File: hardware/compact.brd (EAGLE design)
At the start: 54 x 59 mm, 26 parts, among them SW1 SWITCH_SPDT, U1 MCP73831, U2 EDISON_CONNECTOR_FULLMOUNTING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, U3 EDISON_CONNECTOR_FULLHEADER

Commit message: add USB data lines, use 1.8v line, not vcc, for Max3218, DRC fixes
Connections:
- net 1.8V: now also B78108S1153K.2, C4.1, MAX3218.4, MAX3218.6
- net USB_DN: now also JP1.D-1
- net USB_DP: now also JP1.D+1
- net USB_ID: now also JP1.ID1
- net VSYS: no longer B78108S1153K.2, C4.1, MAX3218.4, MAX3218.6
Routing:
- net 1.8V: track 4.22 -> 47.1 mm
- net USB_ID: track 3.33 -> 42.9 mm
- net USB_DP: track 6.60 -> 45.7 mm, vias 1 -> 2
- net USB_DN: track 9.44 -> 46.3 mm, vias 1 -> 2
- net VSYS: track 96.0 -> 69.9 mm
- net N$11: track 15.8 -> 30.4 mm
- net 1: track 6.96 -> 13.7 mm
- net N$10: track 19.3 -> 16.0 mm
- net VBAT: track 33.8 -> 36.1 mm, vias 1 -> 0
- net T1OUT: track 23.5 -> 24.4 mm
- net GP134_UART_2_RX: track 55.2 -> 56.0 mm
- net 3.3V: track 7.49 -> 8.27 mm
- net N$6: track 3.96 -> 3.33 mm
- net CX: track 35.5 -> 36.0 mm

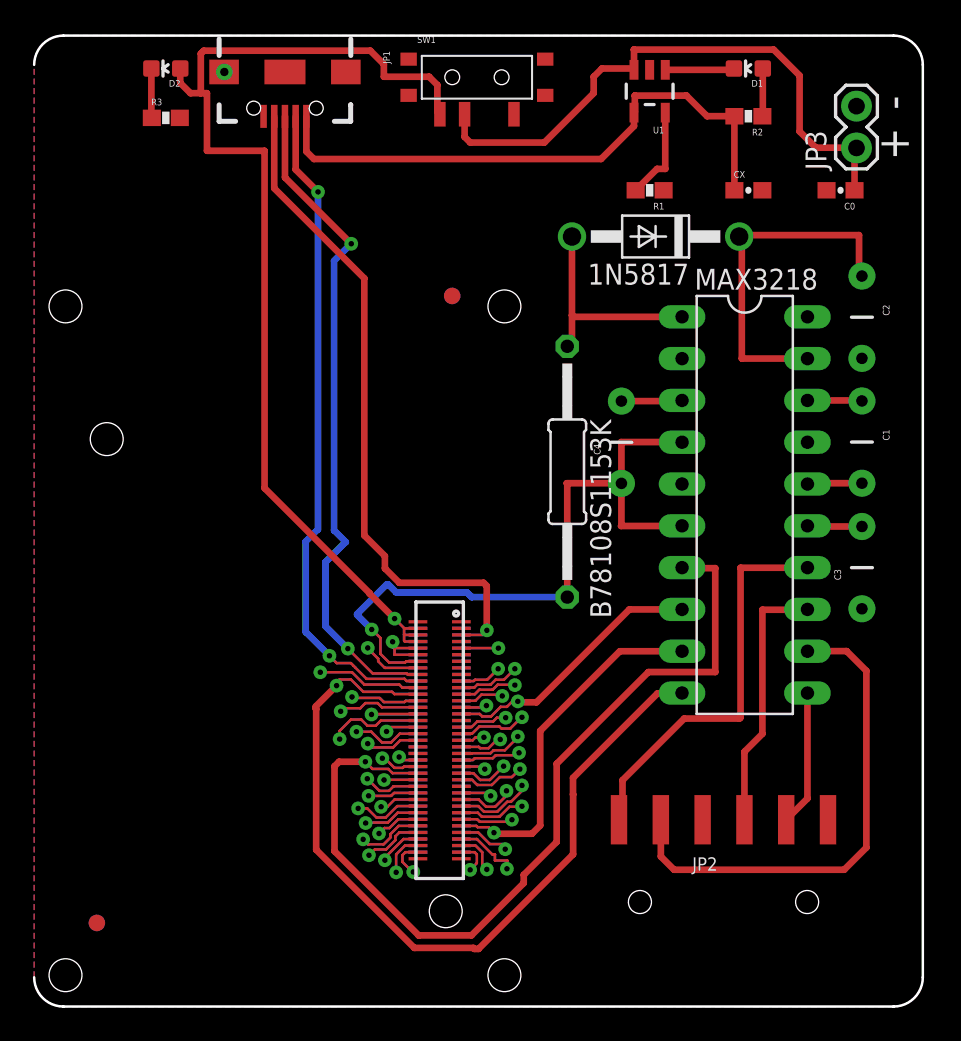
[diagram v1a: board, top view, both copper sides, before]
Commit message: Update readme, board routing fixes, change LED names to functions vice colors
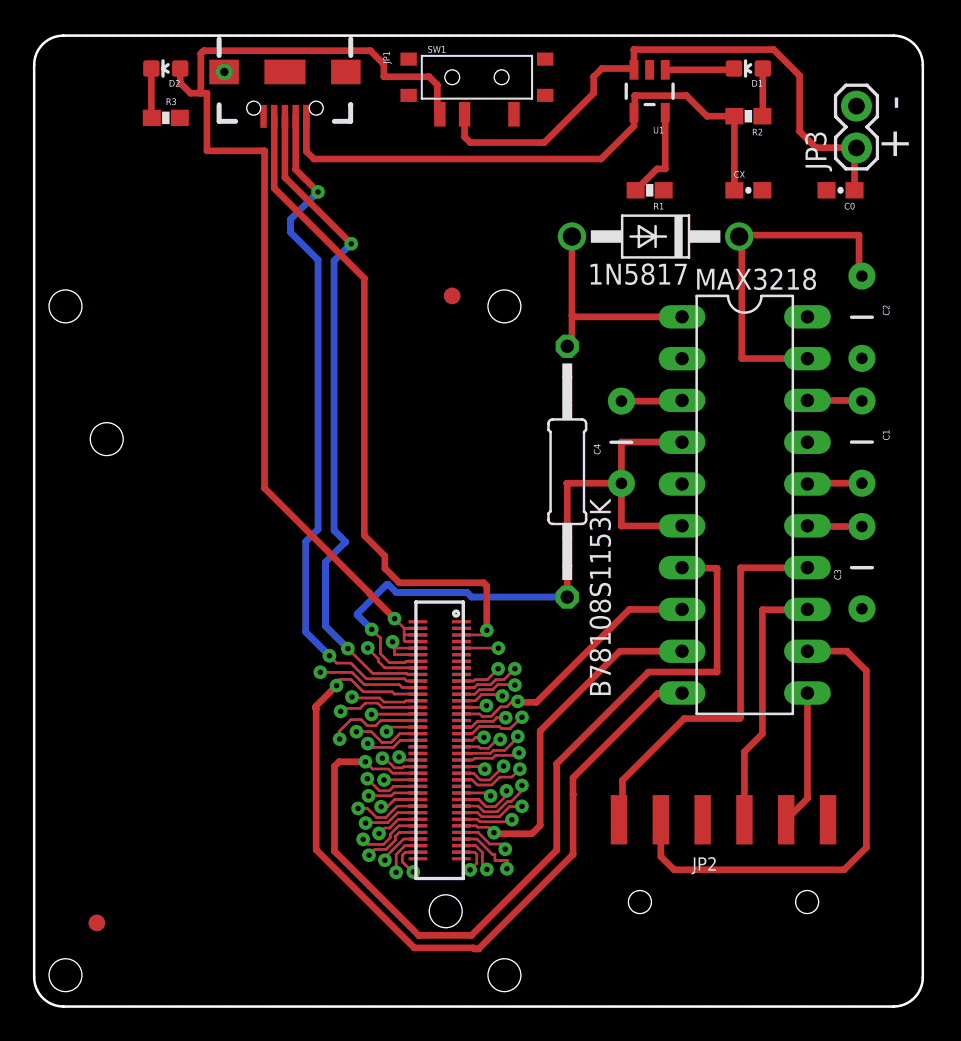
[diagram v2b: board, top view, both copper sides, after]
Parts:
- D1: value RED -> CHARGING
- D2: value BLUE -> POWER
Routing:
- net USB_DN: track 46.3 -> 47.7 mm
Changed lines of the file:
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@@
 <layer number="23" name="tOrigins" color="15" fill="1" visible="yes" active="yes"/>
 <layer number="24" name="bOrigins" color="15" fill="1" visible="yes" active="yes"/>
-<layer number="25" name="tNames" color="7" fill="1" visible="no" active="yes"/>
-<layer number="26" name="bNames" color="7" fill="1" visible="no" active="yes"/>
-<layer number="27" name="tValues" color="7" fill="1" visible="no" active="yes"/>
-<layer number="28" name="bValues" color="7" fill="1" visible="no" active="yes"/>
+<layer number="25" name="tNames" color="7" fill="1" visible="yes" active="yes"/>
+<layer number="26" name="bNames" color="7" fill="1" visible="yes" active="yes"/>
+<layer number="27" name="tValues" color="7" fill="1" visible="yes" active="yes"/>
+<layer number="28" name="bValues" color="7" fill="1" visible="yes" active="yes"/>
 <layer number="29" name="tStop" color="7" fill="3" visible="no" active="yes"/>
 <layer number="30" name="bStop" color="7" fill="6" visible="no" active="yes"/>
@@
 <wire x1="0" y1="59" x2="0" y2="0" width="0.4064" layer="51"/>
 <text x="77.175" y="-57.1375" size="1.778" layer="51">Ben Lamb</text>
+<wire x1="0" y1="57.222" x2="0" y2="1.778" width="0.1524" layer="20"/>
 </plain>
 <attributes>
@@
 <attribute name="PROD_ID" value="CAP-08280" x="43.4" y="49.6" size="1.778" layer="27" display="off"/>
 </element>
-<element name="SW1" library="SparkFun-Electromechanical" package="KPS-1290" value="SWITCH_SPDT" x="26.905" y="56.469" rot="R180">
+<element name="SW1" library="SparkFun-Electromechanical" package="KPS-1290" value="SWITCH_SPDT" x="26.905" y="56.469" smashed="yes" rot="R180">
 <attribute name="PROD_ID" value="SWCH-10651" x="26.905" y="56.469" size="1.778" layer="27" rot="R180" display="off"/>
+<attribute name="NAME" x="25.03625" y="58.361" size="0.4064" layer="25" rot="R180"/>
+<attribute name="VALUE" x="25.58" y="52.58025" size="0.4064" layer="27" rot="R180"/>
 </element>
 <element name="R1" library="SparkFun-Resistors" package="0603-RES" value="2.0k" x="37.4" y="49.6" rot="R180">
 <attribute name="PROD_ID" value="RES-08296" x="37.4" y="49.6" size="1.778" layer="27" rot="R180" display="off"/>
 </element>
-<element name="JP3" library="SparkFun-Connectors" package="1X02" value="M02PTH" x="49.969" y="52.174" rot="R90"/>
+<element name="JP3" library="SparkFun-Connectors" package="1X02" value="M02PTH" x="49.969" y="52.174" smashed="yes" rot="R90">
+<attribute name="NAME" x="48.1402" y="50.8278" size="1.27" layer="25" ratio="10" rot="R90"/>
+</element>
 <element name="R2" library="SparkFun-Resistors" package="0603-RES" value="330" x="43.4" y="54.1" rot="R180">
 <attribute name="PROD_ID" value="RES-00818" x="43.4" y="54.1" size="1.778" layer="27" rot="R180" display="off"/>
 </element>
-<element name="U1" library="SparkFun-PowerIC" package="SOT23-5" value="MCP73831" x="37.4" y="55.62" rot="R180">
+<element name="U1" library="SparkFun-PowerIC" package="SOT23-5" value="MCP73831" x="37.4" y="55.62" smashed="yes" rot="R180">
 <attribute name="PROD_ID" value="IC-09995" x="37.4" y="55.62" size="1.778" layer="27" rot="R180" display="off"/>
+<attribute name="NAME" x="38.289" y="53.461" size="0.4064" layer="25" rot="R180"/>
+<attribute name="VALUE" x="41.83375" y="56.1605" size="0.4064" layer="27" rot="R180"/>
 </element>
-<element name="D1" library="SparkFun-LED" package="LED-0603" value="RED" x="43.4" y="57" rot="R90">
+<element name="D1" library="SparkFun-LED" package="LED-0603" value="CHARGING" x="43.4" y="57" smashed="yes" rot="R90">
 <attribute name="PROD_ID" value="DIO-00819" x="43.4" y="57" size="1.778" layer="27" rot="R90" display="off"/>
+<attribute name="NAME" x="44.289" y="56.3015" size="0.4064" layer="25" rot="R180"/>
+<attribute name="VALUE" x="44.416" y="58.375" size="0.4064" layer="27" rot="R180"/>
 </element>
 <element name="C0" library="SparkFun-Capacitors" package="0603-CAP" value="4.7uF" x="49" y="49.6" rot="R180">
 <attribute name="PROD_ID" value="CAP-08280" x="49" y="49.6" size="1.778" layer="27" rot="R180" display="off"/>
 </element>
-<element name="D2" library="SparkFun-LED" package="LED-0603" value="BLUE" x="8" y="57" rot="R90">
+<element name="D2" library="SparkFun-LED" package="LED-0603" value="POWER" x="8" y="57" smashed="yes" rot="R90">
 <attribute name="PROD_ID" value="DIO-08575" x="8" y="57" size="0.8128" layer="27" font="vector" ratio="15" rot="R90" display="off"/>
+<attribute name="NAME" x="8.889" y="56.3015" size="0.4064" layer="25" rot="R180"/>
+<attribute name="VALUE" x="9.03475" y="58.375" size="0.4064" layer="27" rot="R180"/>
 </element>
-<element name="R3" library="SparkFun-Resistors" package="0603-RES" value="1k" x="8" y="54">
+<element name="R3" library="SparkFun-Resistors" package="0603-RES" value="1k" x="8" y="54" smashed="yes">
 <attribute name="PROD_ID" value="RES-07856" x="8" y="54" size="0.8128" layer="27" font="vector" ratio="15" display="off"/>
+<attribute name="NAME" x="7.9985" y="54.78075" size="0.4064" layer="25" font="vector"/>
+<attribute name="VALUE" x="6.984" y="52.857" size="0.4064" layer="27" font="vector"/>
 </element>
 <element name="FID3" library="SparkFun-Aesthetics" package="FIDUCIAL-1X2" value="FIDUCIAL1X2" x="3.81" y="5.08" rot="MR0"/>
@@
 <element name="C4" library="SparkFun-Capacitors" package="CAP-PTH-5MM" value="1uF" x="35.685" y="34.29" rot="R90"/>
 <element name="1N5817" library="diode" package="DO41-10" value="" x="37.76125" y="46.79" rot="R180"/>
-<element name="B78108S1153K" library="resistor" package="0207/15" value="15uH" x="32.395" y="32.5" rot="R270"/>
+<element name="B78108S1153K" library="resistor" package="0207/15" value="15uH" x="32.395" y="32.5" smashed="yes" rot="R270">
+<attribute name="NAME" x="33.767" y="30.85" size="1.27" layer="25" ratio="10" rot="R270"/>
+<attribute name="VALUE" x="31.7092" y="34.786" size="1.27" layer="27" ratio="10" rot="R270"/>
+</element>
 <element name="C1" library="SparkFun-Capacitors" package="CAP-PTH-5MM" value="0.47uF" x="50.3" y="34.3" rot="R270"/>
 <element name="C3" library="SparkFun-Capacitors" package="CAP-PTH-5MM" value="1uF" x="50.3" y="26.67" rot="R90"/>
-<element name="JP2" library="SparkFun-Connectors" package="1X06-SMD" value="RA 6Pin SMD" x="41.89" y="6.35">
+<element name="JP2" library="SparkFun-Connectors" package="1X06-SMD" value="RA 6Pin SMD" x="41.89" y="6.35" smashed="yes">
 <attribute name="PROD_ID" value="CONN-08971" x="41.89" y="6.35" size="1.778" layer="27" display="off"/>
+<attribute name="NAME" x="39.985" y="8.255" size="0.8128" layer="25"/>
 </element>
-<element name="C2" library="SparkFun-Capacitors" package="CAP-PTH-5MM" value="1uF" x="50.3" y="41.8875" rot="R270"/>
+<element name="C2" library="SparkFun-Capacitors" package="CAP-PTH-5MM" value="1uF" x="50.3" y="41.8875" smashed="yes" rot="R270">
+<attribute name="NAME" x="51.57" y="42.6495" size="0.4064" layer="25" rot="R270"/>
+<attribute name="VALUE" x="48.776" y="42.9035" size="0.4064" layer="27" rot="R270"/>
+</element>
 </elements>
 <signals>
@@
 <wire x1="8.877" y1="57" x2="8.877" y2="56.123" width="0.4064" layer="1"/>
 <wire x1="8.877" y1="56.123" x2="9.5" y2="55.5" width="0.4064" layer="1"/>
-<wire x1="14" y1="52" x2="14" y2="31.5" width="0.4064" layer="1"/>
+<wire x1="14" y1="31.5" x2="14" y2="52" width="0.4064" layer="1"/>
 <wire x1="21.25" y1="56.5" x2="21.25" y2="57.26125" width="0.4064" layer="1"/>
 <wire x1="21.25" y1="57.26125" x2="20.42875" y2="58.0825" width="0.4064" layer="1"/>
@@
 <wire x1="15.89" y1="50.86" x2="17.25" y2="49.5" width="0.4064" layer="1"/>
 <via x="17.25" y="49.5" extent="1-16" drill="0.3302"/>
-<wire x1="17.25" y1="49.5" x2="17.25" y2="29" width="0.4064" layer="16"/>
+<wire x1="17.25" y1="49.5" x2="17.24375" y2="49.5" width="0.4064" layer="16"/>
+<wire x1="17.24375" y1="49.5" x2="15.575" y2="47.83125" width="0.4064" layer="16"/>
+<wire x1="15.575" y1="47.83125" x2="15.575" y2="47.04375" width="0.4064" layer="16"/>
+<wire x1="15.575" y1="47.04375" x2="17.25" y2="45.36875" width="0.4064" layer="16"/>
+<wire x1="17.25" y1="45.36875" x2="17.25" y2="29" width="0.4064" layer="16"/>
 <wire x1="17.25" y1="29" x2="16.5" y2="28.25" width="0.4064" layer="16"/>
 <wire x1="16.5" y1="28.25" x2="16.5" y2="22.75625" width="0.4064" layer="16"/>
@@
 <wire x1="18.25" y1="14.6" x2="18.25" y2="9.4375" width="0.4064" layer="1"/>
 <wire x1="18.25" y1="9.4375" x2="23.3625" y2="4.325" width="0.4064" layer="1"/>
-<wire x1="37.325" y1="20.325" x2="41.3875" y2="20.325" width="0.4064" layer="1"/>
-<wire x1="41.3875" y1="20.325" x2="41.3875" y2="26.6375" width="0.4064" layer="1"/>
+<wire x1="37.325" y1="20.325" x2="41.5" y2="20.325" width="0.4064" layer="1"/>
 <wire x1="41.3875" y1="26.6375" x2="39.4025" y2="26.6375" width="0.4064" layer="1"/>
 <wire x1="39.4025" y1="26.6375" x2="39.37" y2="26.67" width="0.4064" layer="1"/>
 <wire x1="23.3625" y1="4.3125" x2="23.3625" y2="4.325" width="0.4064" layer="1"/>
 <wire x1="37.325" y1="20.325" x2="31.75" y2="14.75" width="0.4064" layer="1"/>
-<wire x1="31.75" y1="14.75" x2="31.75" y2="10" width="0.4064" layer="1"/>
-<wire x1="31.75" y1="10" x2="29.75" y2="8" width="0.4064" layer="1"/>
-<wire x1="29.75" y1="8" x2="29.75" y2="7.5" width="0.4064" layer="1"/>
-<wire x1="29.75" y1="7.5" x2="26.575" y2="4.325" width="0.4064" layer="1"/>
+<wire x1="31.75" y1="14.75" x2="31.75" y2="9.5" width="0.4064" layer="1"/>
+<wire x1="31.75" y1="9.5" x2="26.575" y2="4.325" width="0.4064" layer="1"/>
 <wire x1="26.575" y1="4.325" x2="23.3625" y2="4.325" width="0.4064" layer="1"/>
+<wire x1="41.5" y1="20.325" x2="41.5" y2="26.63125" width="0.4064" layer="1"/>
+<wire x1="41.5" y1="26.63125" x2="41.3875" y2="26.63125" width="0.4064" layer="1"/>
+<wire x1="41.3875" y1="26.63125" x2="41.3875" y2="26.6375" width="0.4064" layer="1"/>
 </signal>
 <signal name="N$15">
